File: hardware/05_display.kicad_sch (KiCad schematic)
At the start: 0 parts

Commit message: Display sheet: panel connector, touch, backlight
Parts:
- added J10: LINK2, Package_LCC:PLCC-44_16.6x16.6mm_P1.27mm, symbol Connector_Generic:Conn_01x02
- added J5: LCD_AFY800480_40P, Package_LCC:PLCC-84_29.3x29.3mm_P1.27mm, symbol oscil:LCD_AFY800480_40P
- added J6: GT911_TOUCH_6P, symbol oscil:GT911_TOUCH_6P
- added J7: XL6009_IN, Package_LCC:PLCC-44_16.6x16.6mm_P1.27mm, symbol Connector_Generic:Conn_01x02
- added J8: XL6009_OUT, Package_LCC:PLCC-44_16.6x16.6mm_P1.27mm, symbol Connector_Generic:Conn_01x02
- added J9: LINK1, Package_LCC:PLCC-44_16.6x16.6mm_P1.27mm, symbol Connector_Generic:Conn_01x03
- added R15, R16, R17, R18: 10k, symbol Device:R
- added R19, R20: 4.7k, symbol Device:R
- added R21: 75R, symbol Device:R
- added U8: ESP32-S3-N16R8-DEVBOARD, RF_Module:ESP32-S2-MINI-1, symbol oscil:ESP32-S3-N16R8-DEVBOARD
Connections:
- new net: J8.1 (Pin_1), R21.2
- new net: J5.36 (SPI_MOSI), R17.2
- new net: J5.31 (DISP), R16.2
- new net: J5.3 (~{SPI_CS}), R15.2
- new net: J5.35 (SPI_SCK), R18.2
- new net +3V3_DISP: J5.4 (VDD), J6.4 (VDD), R15.1, R16.1, R19.2, R20.2, U8.1 (3V3)
- new net +5V: J7.1 (Pin_1), U8.21 (5V)
- new net GND: J10.2 (Pin_2), J5.1 (LEDK), J5.13 (G0), J5.14 (G1), J5.21 (B0), J5.22 (B1), J5.23 (B2), J5.29 (GND), J5.5 (R0), J5.6 (R1), J5.7 (R2), J6.1 (GND), J7.2 (Pin_2), J8.2 (Pin_2), J9.3 (Pin_3), R17.1, R18.1, U8.22 (GND), U8.23 (GND), U8.24 (GND), U8.44 (GND)
- new net LCD_B3: J5.24 (B3), U8.19 (IO13)
- new net LCD_B4: J5.25 (B4), U8.20 (IO14)
- new net LCD_B5: J5.26 (B5), U8.8 (IO15)
- new net LCD_B6: J5.27 (B6), U8.9 (IO16)
- new net LCD_B7: J5.28 (B7), U8.10 (IO17)
- new net LCD_DCLK: J5.30 (DCLK), U8.11 (IO18)
- new net LCD_DE: J5.34 (DE), U8.36 (IO39)
- new net LCD_G2: J5.15 (G2), U8.7 (IO7)
- new net LCD_G3: J5.16 (G3), U8.12 (IO8)
- new net LCD_G4: J5.17 (G4), U8.15 (IO9)
- new net LCD_G5: J5.18 (G5), U8.16 (IO10)
- new net LCD_G6: J5.19 (G6), U8.17 (IO11)
- new net LCD_G7: J5.20 (G7), U8.18 (IO12)
- new net LCD_HSYNC: J5.32 (HSYNC), U8.27 (IO21)
- new net LCD_R3: J5.8 (R3), U8.41 (IO1)
- new net LCD_R4: J5.9 (R4), U8.40 (IO2)
- new net LCD_R5: J5.10 (R5), U8.4 (IO4)
- new net LCD_R6: J5.11 (R6), U8.5 (IO5)
- new net LCD_R7: J5.12 (R7), U8.6 (IO6)
- new net LCD_VSYNC: J5.33 (VSYNC), U8.35 (IO38)
- new net LEDA: J5.2 (LEDA), R21.1
- new net LINK1_RX: J9.2 (Pin_2), U8.42 (IO44_RX)
- new net LINK1_TX: J9.1 (Pin_1), U8.43 (IO43_TX)
- new net LINK2_TX: J10.1 (Pin_1), U8.28 (IO47)
- new net TOUCH_INT: J6.2 (CHG_INT), U8.39 (IO42)
- new net TOUCH_RESET: J6.3 (~{RESET}), U8.29 (IO48_RGB)
- new net TOUCH_SCL: J6.5 (SCL), R19.1, U8.38 (IO41)
- new net TOUCH_SDA: J6.6 (SDA), R20.1, U8.37 (IO40)
- no-connect marks 0 -> 15
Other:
- note added: "Backlight: 8 LEDs x 3 strings, ~25.6V at 60mA. Adafruit 1932 driver tops out at 24V/7 LEDs, so XL6009 instead. Set module to ~30V by trimpot: 25.6V + 60mA x 75R."
- note added: "DISP tied high: display always on, saves a GPIO. Deliberate. Panel SPI (CS/SCL/SDA) tied off, no pins left on board 2. If the panel stays blank at bring-up, it may need SPI init. HSYNC/VSYNC negative polarity per datasheet p.9."
- note added: "INT must be driveable: GT911 reads it at reset to set its I2C address. RESET shares IO48 with the onboard WS2812; asserts once at boot. 4.7k pull-ups; go smaller if 400kHz is flaky (GT911 Programming Guide, communication section)."
- note added: "LINK2 is TX only. Board 3 sends nothing back. This is what fits board 2 into 27 pins."
- note added: "Unused LSBs (R0-R2, G0-G1, B0-B2) tied low. RGB565 drives the top 5/6/5 bits; floating inputs would flicker."

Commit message: Add final Rev A schematic PDF and edited footprints
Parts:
- J10, J7, J8: footprint Package_LCC:PLCC-44_16.6x16.6mm_P1.27mm -> Connector_PinHeader_2.54mm:PinHeader_1x02_P2.54mm_Vertical
- J9: footprint Package_LCC:PLCC-44_16.6x16.6mm_P1.27mm -> Connector:FanPinHeader_1x03_P2.54mm_Vertical
- R15, R16, R17, R18, R19, R20, R21: footprint (none) -> Resistor_THT:R_Axial_DIN0207_L6.3mm_D2.5mm_P10.16mm_Horizontal
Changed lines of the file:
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@@
 	(title_block
 		(title "Oscil")
-		(date "2026-09-18")
-		(rev "0.1")
+		(date "2026-09-21")
+		(rev "A")
 		(comment 1 "Two-channel Digital Oscilloscope and Function Generator")
 		(comment 2 "ESP32-S3 / ESP-IDF / FreeRTOS")
@@
 			)
 		)
-		(property "Footprint" "Package_LCC:PLCC-44_16.6x16.6mm_P1.27mm"
+		(property "Footprint" "Connector_PinHeader_2.54mm:PinHeader_1x02_P2.54mm_Vertical"
 			(at 222.25 90.17 0)
 			(hide yes)
@@
 			)
 		)
-		(property "Footprint" ""
+		(property "Footprint" "Resistor_THT:R_Axial_DIN0207_L6.3mm_D2.5mm_P10.16mm_Horizontal"
 			(at 234.95 67.818 90)
 			(hide yes)
@@
 			)
 		)
-		(property "Footprint" "Package_LCC:PLCC-44_16.6x16.6mm_P1.27mm"
+		(property "Footprint" "Connector_PinHeader_2.54mm:PinHeader_1x02_P2.54mm_Vertical"
 			(at 260.35 90.17 0)
 			(hide yes)
@@
 			)
 		)
-		(property "Footprint" "Package_LCC:PLCC-44_16.6x16.6mm_P1.27mm"
+		(property "Footprint" "Connector:FanPinHeader_1x03_P2.54mm_Vertical"
 			(at 229.87 121.92 0)
 			(hide yes)
@@
 			)
 		)
-		(property "Footprint" ""
+		(property "Footprint" "Resistor_THT:R_Axial_DIN0207_L6.3mm_D2.5mm_P10.16mm_Horizontal"
 			(at 234.95 77.978 90)
 			(hide yes)
@@
 			)
 		)
-		(property "Footprint" "Package_LCC:PLCC-44_16.6x16.6mm_P1.27mm"
+		(property "Footprint" "Connector_PinHeader_2.54mm:PinHeader_1x02_P2.54mm_Vertical"
 			(at 261.62 120.65 0)
 			(hide yes)
@@
 			)
 		)
-		(property "Footprint" ""
+		(property "Footprint" "Resistor_THT:R_Axial_DIN0207_L6.3mm_D2.5mm_P10.16mm_Horizontal"
 			(at 168.91 46.228 90)
 			(hide yes)
@@
 			)
 		)
-		(property "Footprint" ""
+		(property "Footprint" "Resistor_THT:R_Axial_DIN0207_L6.3mm_D2.5mm_P10.16mm_Horizontal"
 			(at 250.19 91.948 90)
 			(hide yes)
@@
 			)
 		)
-		(property "Footprint" ""
+		(property "Footprint" "Resistor_THT:R_Axial_DIN0207_L6.3mm_D2.5mm_P10.16mm_Horizontal"
 			(at 180.34 58.928 90)
 			(hide yes)
@@
 			)
 		)
-		(property "Footprint" ""
+		(property "Footprint" "Resistor_THT:R_Axial_DIN0207_L6.3mm_D2.5mm_P10.16mm_Horizontal"
 			(at 111.76 41.148 90)
 			(hide yes)
@@
 			)
 		)
-		(property "Footprint" ""
+		(property "Footprint" "Resistor_THT:R_Axial_DIN0207_L6.3mm_D2.5mm_P10.16mm_Horizontal"
 			(at 168.91 48.768 90)
 			(hide yes)

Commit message: hardware: display sheet relabelled to the new LCD pin order, schematic exports regenerated
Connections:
- net LCD_B3: now also U8.7 (IO7); no longer U8.19 (IO13)
- net LCD_B4: now also U8.8 (IO15); no longer U8.20 (IO14)
- net LCD_B5: now also U8.9 (IO16); no longer U8.8 (IO15)
- net LCD_B6: now also U8.10 (IO17); no longer U8.9 (IO16)
- net LCD_B7: now also U8.11 (IO18); no longer U8.10 (IO17)
- net LCD_DCLK: now also U8.20 (IO14); no longer U8.11 (IO18)
- net LCD_G2: now also U8.12 (IO8); no longer U8.7 (IO7)
- net LCD_G3: now also U8.15 (IO9); no longer U8.12 (IO8)
- net LCD_G4: now also U8.16 (IO10); no longer U8.15 (IO9)
- net LCD_G5: now also U8.17 (IO11); no longer U8.16 (IO10)
- net LCD_G6: now also U8.18 (IO12); no longer U8.17 (IO11)
- net LCD_G7: now also U8.19 (IO13); no longer U8.18 (IO12)
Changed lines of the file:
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@@
 		)
 	)
-	(label "LCD_B7"
+	(label "LCD_B6"
 		(at 34.29 54.61 180)
 		(effects
@@
 		)
 	)
-	(label "LCD_B5"
+	(label "LCD_B4"
 		(at 34.29 49.53 180)
 		(effects
@@
 		)
 	)
-	(label "LCD_G4"
+	(label "LCD_G3"
 		(at 34.29 67.31 180)
 		(effects
@@
 		)
 	)
-	(label "LCD_G3"
+	(label "LCD_G2"
 		(at 34.29 59.69 180)
 		(effects
@@
 		)
 	)
-	(label "LCD_G5"
+	(label "LCD_G4"
 		(at 34.29 69.85 180)
 		(effects
@@
 		)
 	)
-	(label "LCD_DCLK"
+	(label "LCD_B7"
 		(at 34.29 57.15 180)
 		(effects
@@
 		)
 	)
-	(label "LCD_B4"
+	(label "LCD_DCLK"
 		(at 34.29 80.01 180)
 		(effects
@@
 		)
 	)
-	(label "LCD_G6"
+	(label "LCD_G5"
 		(at 34.29 72.39 180)
 		(effects
@@
 		)
 	)
-	(label "LCD_G7"
+	(label "LCD_G6"
 		(at 34.29 74.93 180)
 		(effects
@@
 		)
 	)
-	(label "LCD_G2"
+	(label "LCD_B3"
 		(at 34.29 46.99 180)
 		(effects
@@
 		)
 	)
-	(label "LCD_B6"
+	(label "LCD_B5"
 		(at 34.29 52.07 180)
 		(effects
@@
 		)
 	)
-	(label "LCD_B3"
+	(label "LCD_G7"
 		(at 34.29 77.47 180)
 		(effects

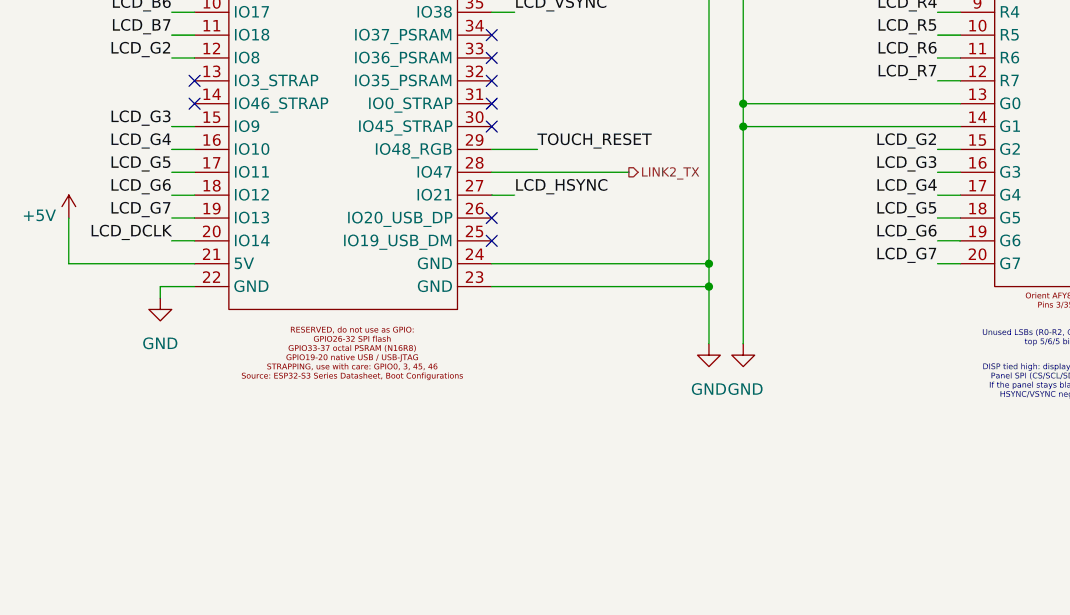
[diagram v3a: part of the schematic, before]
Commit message: hardware: 220R series on each link line, analog decoupling notes
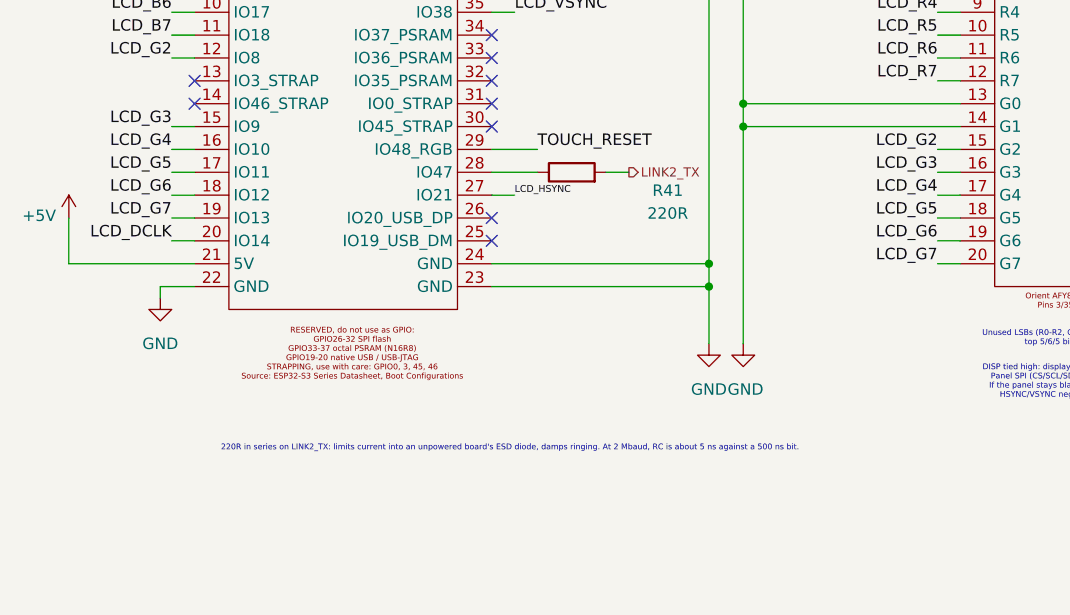
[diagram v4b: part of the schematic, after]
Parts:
- added R41: 220R, symbol Device:R
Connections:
- net LINK2_TX: now also R41.2; no longer U8.28 (IO47)
- new net: R41.1, U8.28 (IO47)
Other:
- note added: "220R in series on LINK2_TX: limits current into an unpowered board's ESD diode, damps ringing. At 2 Mbaud, RC is about 5 ns against a 500 ns bit."
